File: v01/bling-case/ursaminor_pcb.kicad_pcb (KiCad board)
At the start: 2 copper layers, 298.8 x 122 mm, 232 parts, among them J1 USB_C_Receptacle_USB2.0, J2 I2C-L, J3 I2C-R, J4 AVR-ISP-6, SW1 Reset, U1 ATmega32U4-AU, U2 MCP23017_SO, U3 IS31FL3733-TQ, U4 HOLE, U4 IS31FL3733-TQ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

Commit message: Start working on bling-base
* Use north face LEDS as south facing ones have a tendency to shine in
  my eyes.
* Import the board outline from onshape.
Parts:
- removed D106: 6028 LED, v01:RGB_3528_Blue_Notch-MX
- removed the G*** at (163.1, 69.0)
- removed the G*** at (163.1, 69.5)
- removed REF** (x8): breakaway-mousebites, Keebio-Parts:breakaway-mousebites
- removed REF** (x8): MountingHole_2.2mm_M2_DIN965_Pad, MountingHole:MountingHole_2.2mm_M2_DIN965_Pad
- removed REF**: 1U, Keebio-Parts:MX-Alps-Choc-1U
- removed the U4 at (162.8, 89.0)
- moved D58 0.53 mm to (80.5, 25.8), turned to 0 degrees
- moved D80 0.19 mm to (42.4, 75.2), turned to 0 degrees
- moved D100 0.15 mm to (265.2, 87.0)
- moved D64 0.15 mm to (265.1, 30.0)
- moved D65 0.15 mm to (284.2, 37.2)
- moved D66 0.15 mm to (303.1, 37.2)
- moved D108 0.15 mm to (221.1, 108.5)
- moved D61 0.15 mm to (208.1, 32.4)
- moved D63 0.15 mm to (246.3, 25.3)
- moved D73 0.15 mm to (208.0, 51.4)
- moved D74 0.15 mm to (227.2, 49.0)
- moved D75 0.15 mm to (246.2, 44.3)
- moved D86 0.15 mm to (227.2, 68.0)
- moved D87 0.15 mm to (246.2, 63.3)
- moved D97 0.15 mm to (208.1, 89.4)
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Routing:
- net GND: track 316.9 -> 1.41 mm, vias 93 -> 0
- net +5V: track 305.3 -> 0.00 mm, vias 13 -> 0
- net Left-SW1: track 253.2 -> 0.00 mm, vias 2 -> 0
- net Left-SW2: track 223.7 -> 0.00 mm, vias 9 -> 0
- net Col0: track 218.1 -> 0.00 mm, vias 3 -> 0
- net Left-SW3: track 217.9 -> 0.00 mm, vias 11 -> 0
- net Col1: track 201.2 -> 0.00 mm, vias 4 -> 0
- net Left-SW8: track 197.1 -> 0.00 mm, vias 14 -> 0
- net Left-SW11: track 193.0 -> 0.00 mm, vias 13 -> 0
- net Left-SW10: track 188.1 -> 0.00 mm, vias 2 -> 0
- net Left-SW12: track 185.7 -> 0.00 mm, vias 8 -> 0
- net SCL-L: track 183.5 -> 0.00 mm, vias 5 -> 0
- net Left-SW7: track 180.0 -> 0.00 mm, vias 2 -> 0
- net SDA-L: track 179.0 -> 0.00 mm, vias 5 -> 0
- net Left-SW9: track 176.2 -> 0.00 mm, vias 4 -> 0
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- removed copper zone on B.Cu, net (none)
- removed copper zone on F.Cu, net (none)
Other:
- board size 298.8 x 122 mm -> 298.6 x 118.1 mm

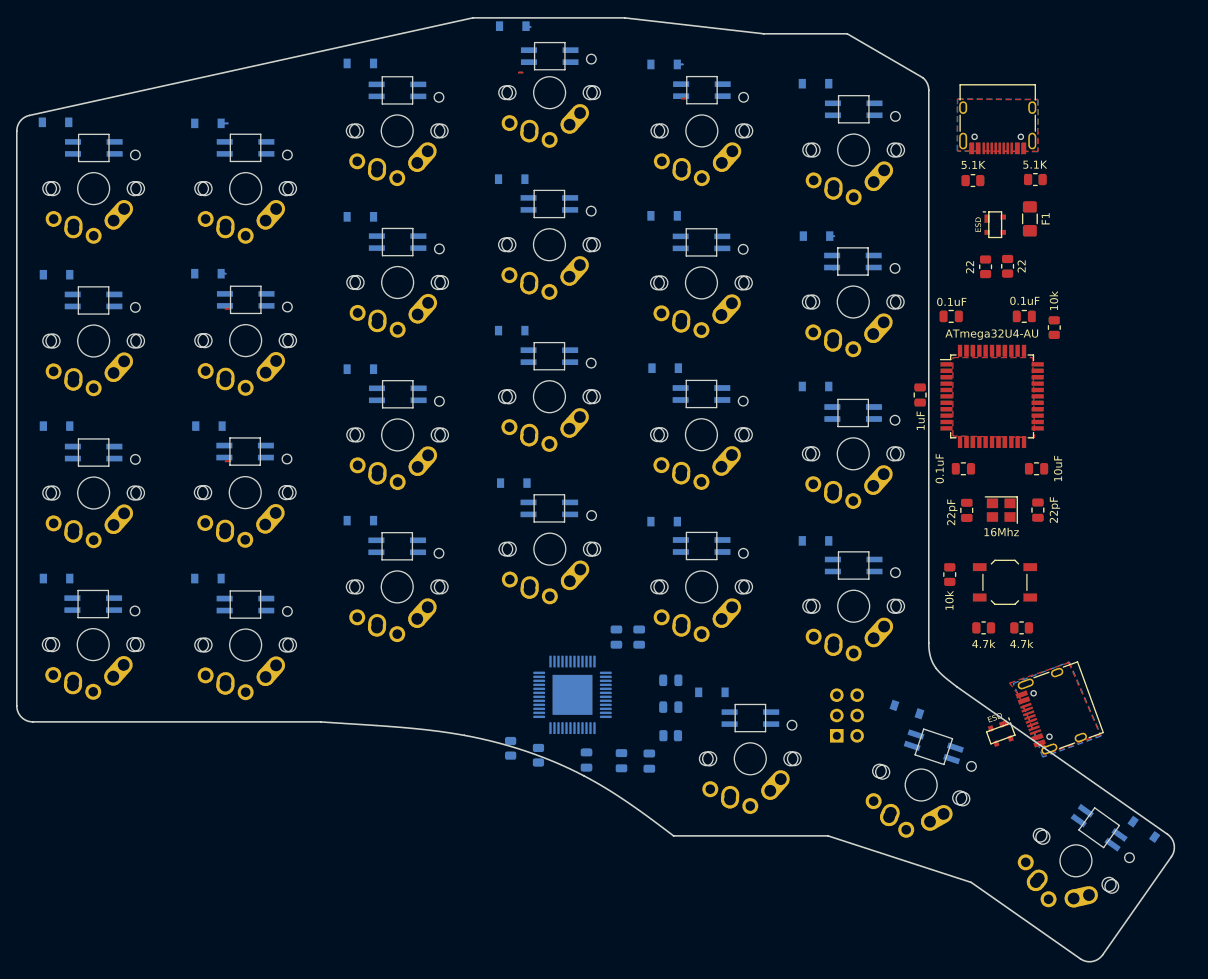
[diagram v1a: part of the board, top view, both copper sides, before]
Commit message: Get left side components placed
Routing is going to be tricky but it still seems doable.
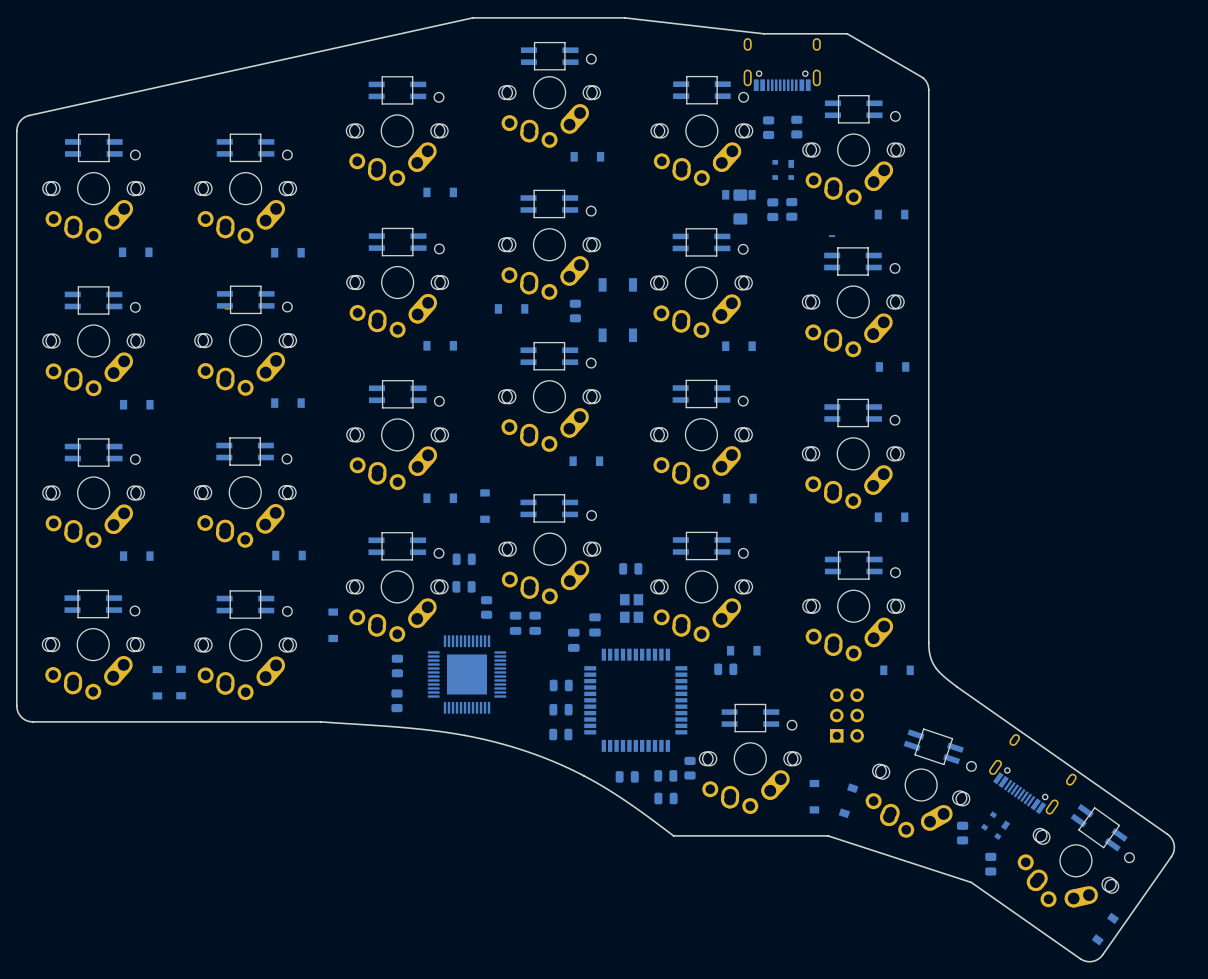
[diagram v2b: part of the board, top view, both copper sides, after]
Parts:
- removed G***: LOGO, v01:constellation-left-rgb
- C1, C2, C3, C4, C5, C6, C7, F1, J1, J2, R1, R2, R3, R4, R5, R6, R7, R8, SW1, U1, U5, U6, Y1: moved to B.Cu
- moved C4 72.9 mm to (95.0, 110.7), turned to 180 degrees
- moved R8 71.5 mm to (98.0, 109.7), turned to 90 degrees
- moved C6 69.7 mm to (69.8, 87.0), turned to 180 degrees
- moved C7 68.1 mm to (81.9, 105.5)
- moved SW1 59.2 mm to (89.0, 52.4), turned to 90 degrees
- moved U1 58.5 mm to (91.3, 101.2)
- moved C3 57.7 mm to (82.0, 99.3), turned to 180 degrees
- moved R1 57.2 mm to (83.7, 52.5), turned to 90 degrees
- moved C1 51.4 mm to (90.7, 84.8), turned to 180 degrees
- moved C2 48.6 mm to (86.2, 91.8), turned to 270 degrees
- moved Y1 47.8 mm to (90.8, 89.7), turned to 270 degrees
- moved C5 38.9 mm to (102.5, 97.3)
- moved F1 36.2 mm to (104.3, 39.5), turned to 270 degrees
- moved R14 35.3 mm to (61.5, 96.9), turned to 270 degrees
- moved R2 34.0 mm to (107.9, 29.6), turned to 90 degrees
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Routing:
- net GND: track 1.41 -> 0.00 mm
- net Net-(D5-Pad2): track 1.30 -> 0.00 mm
- net Net-(D2-Pad2): track 0.82 -> 0.00 mm
- net (no net): track 0.60 -> 0.00 mm
- net Net-(D8-Pad2): track 1.17 -> 0.60 mm
- removed copper zone on B.Cu, net GND
- removed copper zone on F.Cu, net GND

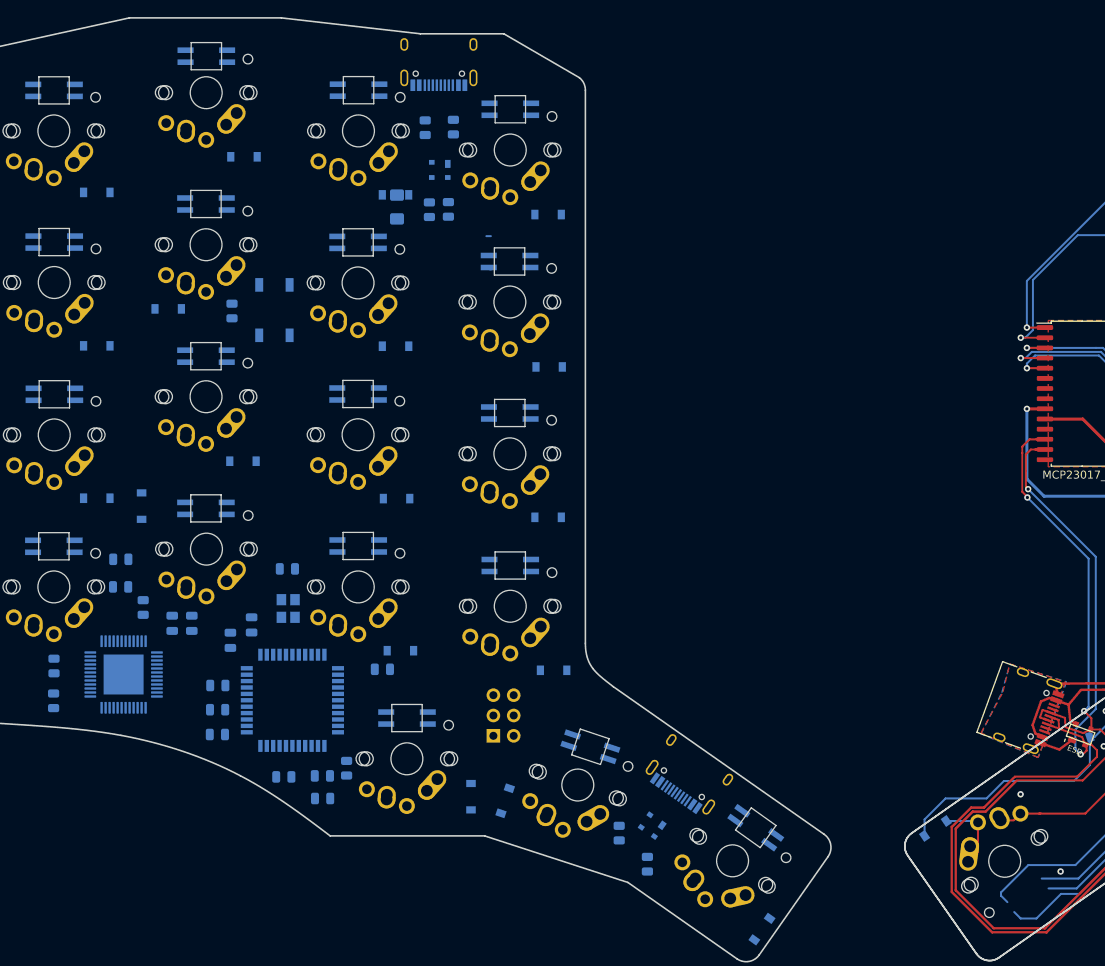
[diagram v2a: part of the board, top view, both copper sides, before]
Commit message: Improve component layout and start routing traces.
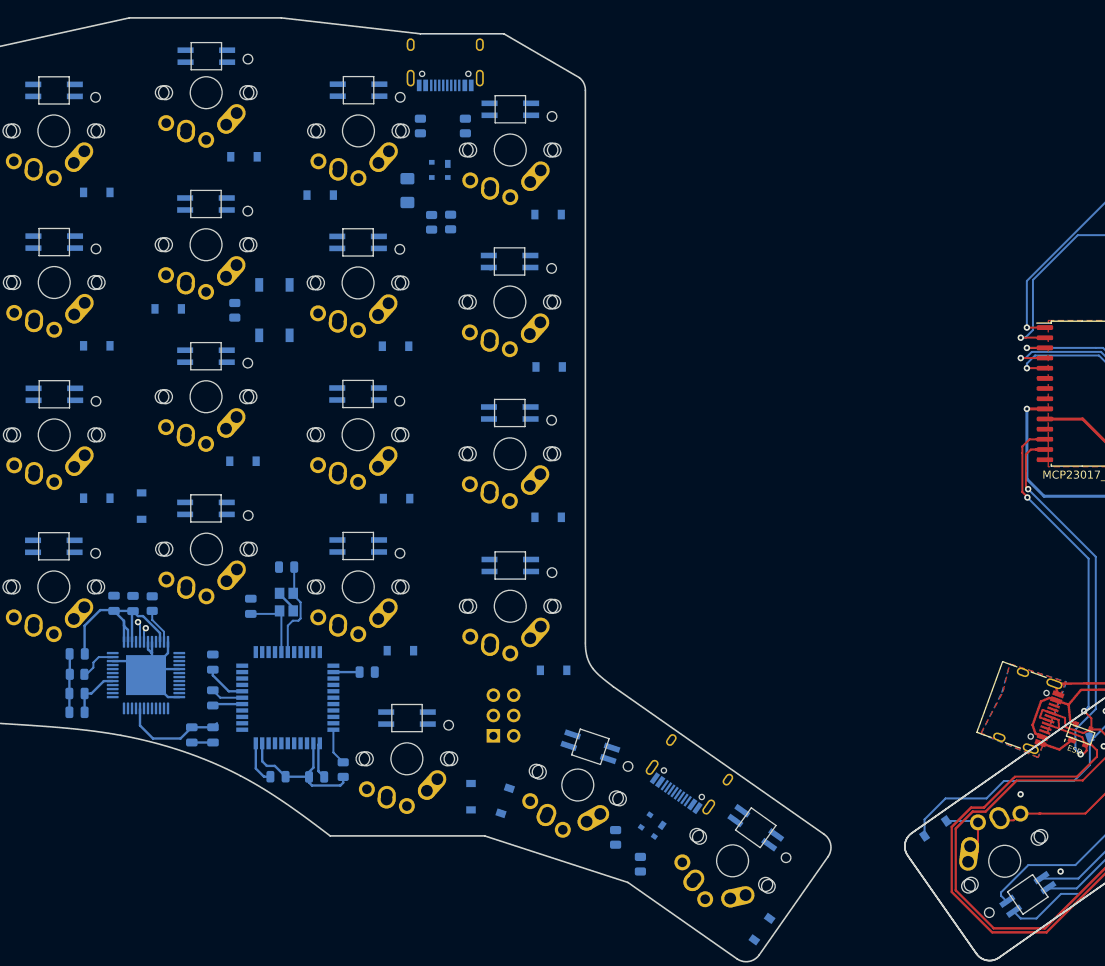
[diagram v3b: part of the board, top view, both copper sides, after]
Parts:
- removed R11: 100K, Resistor_SMD:R_0805_2012Metric
- added D106: 6028 LED, v01:RGB_3528_Blue_Notch-MX, B.Cu at (180.3, 121.3)
- moved C6 30.8 mm to (89.5, 110.8), turned to 0 degrees
- moved C19 27.9 mm to (64.3, 100.3), turned to 0 degrees
- moved C13 19.9 mm to (64.3, 102.7)
- moved C11 19.2 mm to (64.4, 95.4), turned to 0 degrees
- moved C12 15.8 mm to (81.3, 105.5), turned to 90 degrees
- moved C17 10.0 mm to (69.0, 89.1), turned to 90 degrees
- moved D5 9.42 mm to (94.8, 38.0)
- moved C7 9.07 mm to (81.3, 96.4), turned to 90 degrees
- moved C21 5.49 mm to (71.3, 89.1), turned to 270 degrees
- moved C18 4.51 mm to (78.7, 105.5), turned to 90 degrees
- moved R14 3.07 mm to (64.4, 98.0), turned to 180 degrees
- moved U4 2.80 mm to (73.0, 98.0)
- moved F1 2.43 mm to (105.7, 37.5), turned to 90 degrees
- moved C2 2.33 mm to (86.1, 89.5), turned to 90 degrees
- moved C5 1.93 mm to (100.6, 97.7)
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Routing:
- net +5V: track 0.00 -> 65.4 mm
- net GND: track 0.00 -> 60.8 mm
- net Net-(C1-Pad1): track 0.00 -> 12.1 mm
- net Net-(C2-Pad1): track 0.00 -> 9.00 mm
- net Net-(R12-Pad1): track 0.00 -> 5.28 mm
- net Net-(R14-Pad1): track 0.00 -> 4.79 mm
- net Net-(R8-Pad2): track 0.00 -> 4.58 mm
- net Net-(C3-Pad1): track 0.00 -> 4.06 mm
- net SCL-L: track 0.00 -> 3.19 mm, vias 0 -> 1
- net SDA-L: track 0.00 -> 2.57 mm, vias 0 -> 1
- net Net-(D12-Pad2): track 0.57 -> 0.00 mm

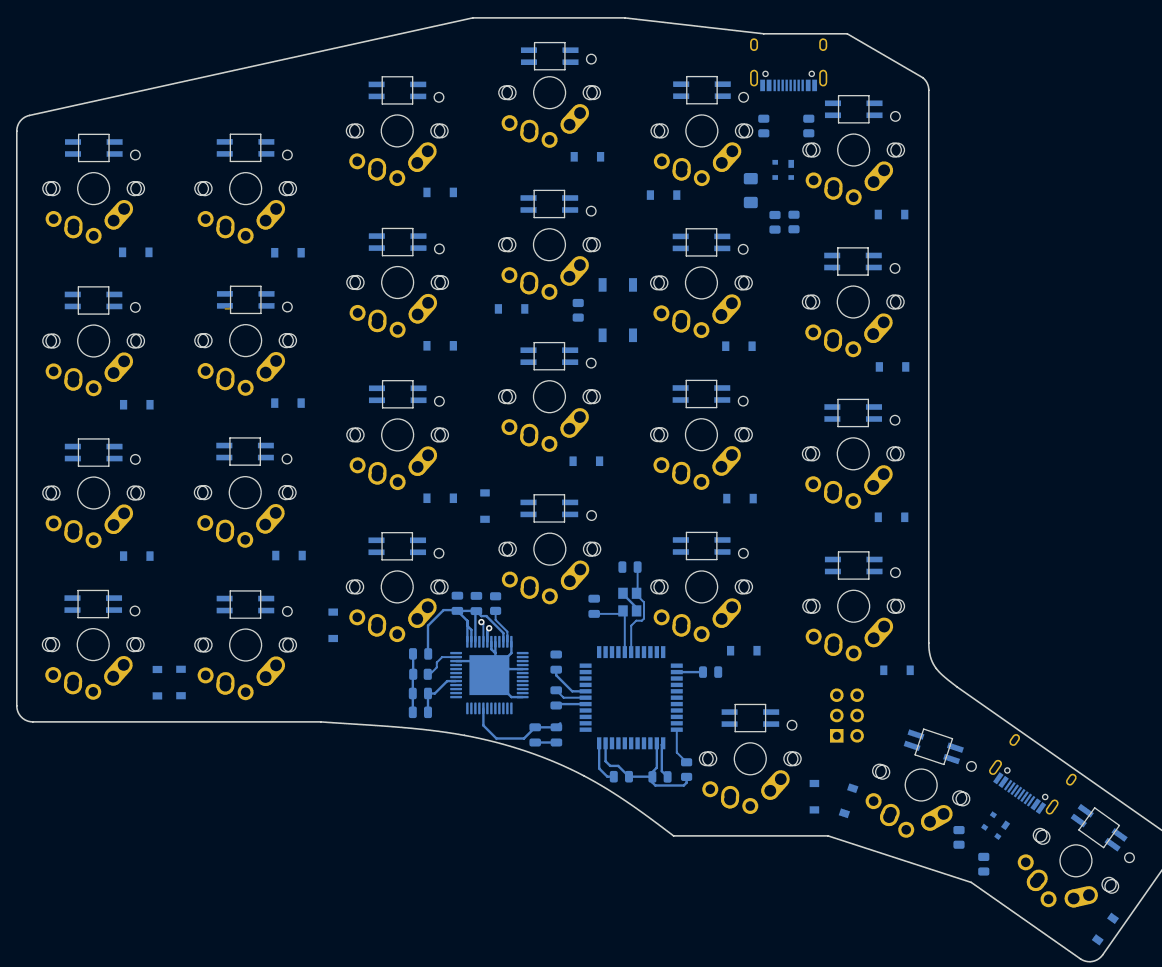
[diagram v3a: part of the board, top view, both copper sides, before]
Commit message: More routing on the left side
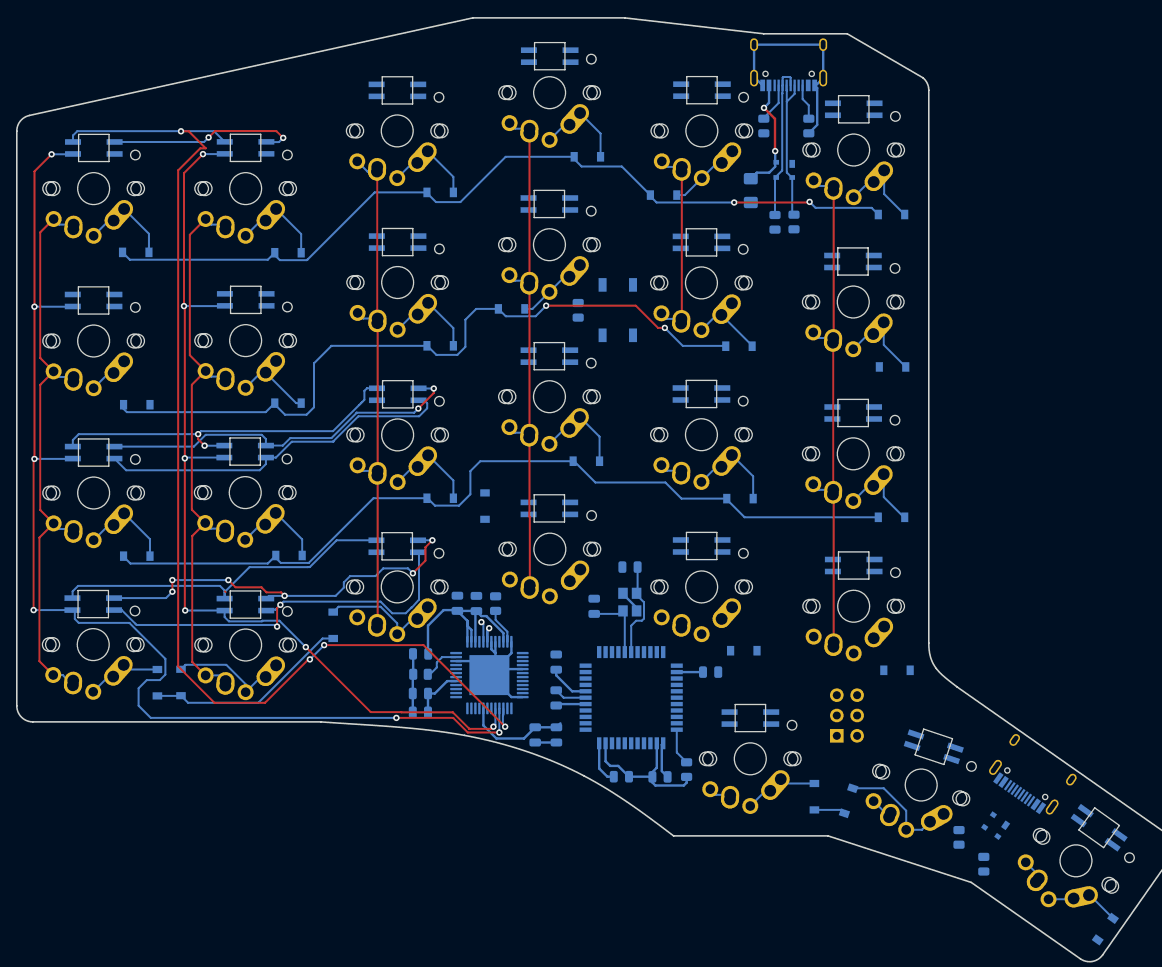
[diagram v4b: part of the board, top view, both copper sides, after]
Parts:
- moved U5 0.12 mm to (109.8, 34.9)
- turned R4 to 270 degrees
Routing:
- net Left-CS1: track 0.00 -> 147.5 mm, vias 0 -> 6
- net Left-SW12: track 0.00 -> 144.0 mm, vias 0 -> 4
- net Left-CS2: track 0.00 -> 118.7 mm, vias 0 -> 6
- net Row2-L: track 0.00 -> 106.4 mm
- net Row0-L: track 0.00 -> 105.5 mm, vias 0 -> 2
- net Row1-L: track 0.00 -> 91.8 mm, vias 0 -> 2
- net Col1: track 0.00 -> 72.9 mm
- net Col0: track 0.00 -> 72.8 mm
- net Col5: track 0.00 -> 68.4 mm
- net Col3: track 0.00 -> 67.7 mm
- net Col2: track 0.00 -> 66.2 mm
- net Left-SW2: track 0.00 -> 51.4 mm, vias 0 -> 6
- net Left-SW1: track 0.00 -> 51.3 mm, vias 0 -> 2
- net Left-SW5: track 0.00 -> 46.8 mm, vias 0 -> 2
- net Left-SW6: track 0.00 -> 46.5 mm, vias 0 -> 2
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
